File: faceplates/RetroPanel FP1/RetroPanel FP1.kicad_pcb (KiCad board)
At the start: 2 copper layers, 101.5 x 25 mm, 10 parts, among them M1 Mounting_Pin, M10 Mounting_Pad, M2 Mounting_Pin, M3 Mounting_Pin, M4 Mounting_Pin, M5 Mounting_Pad, M6 Mounting_Pad, M7 Mounting_Pad, M8 Mounting_Pad, M9 Mounting_Pad

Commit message: FP1 icons
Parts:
- added G***: LOGO, RetroPanel:logo_small, F.Cu at (150.8, 102.3)
- added G***: LOGO, RetroPanel:icon_extra, F.Cu at (173.5, 97.0)
- added G***: LOGO, RetroPanel:icon_hdd, F.Cu at (177.2, 82.9)
- added G***: LOGO, RetroPanel:icon_running, F.Cu at (120.6, 82.9)
- added G***: LOGO, RetroPanel:icon_slow, F.Cu at (188.2, 82.9)
- added G***: LOGO, RetroPanel:icon_turbo, F.Cu at (184.6, 97.0)
- added G***: LOGO, RetroPanel:icon_power, F.Cu at (116.9, 97.0)
- added G***: LOGO, RetroPanel:icon_reset, F.Cu at (127.9, 97.0)
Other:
- board text removed: "EXTRA"
- board text removed: "POWER"
- board text removed: "RESET"
- board text removed: "TURBO"

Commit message: Export files
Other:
- board text added: "JLCJLCJLCJLC"

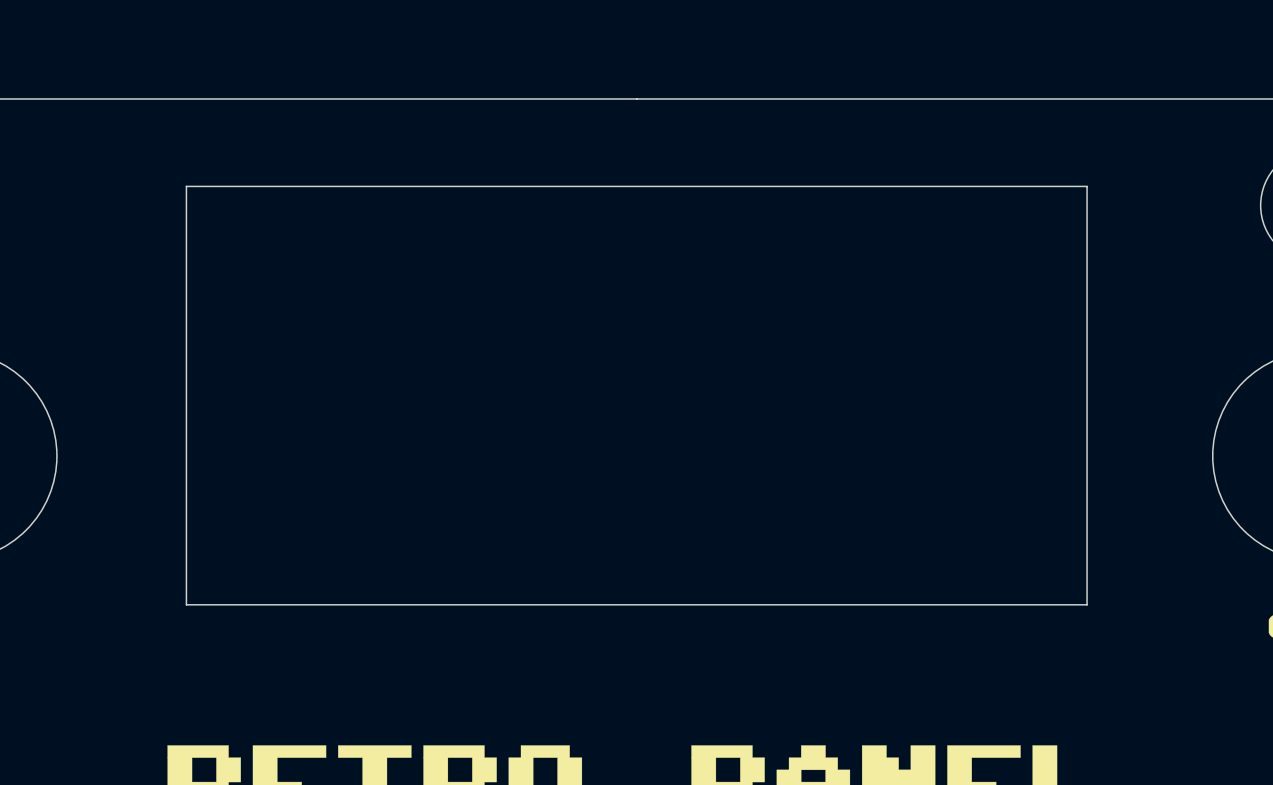
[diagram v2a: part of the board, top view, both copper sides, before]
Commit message: Tweak display cutout
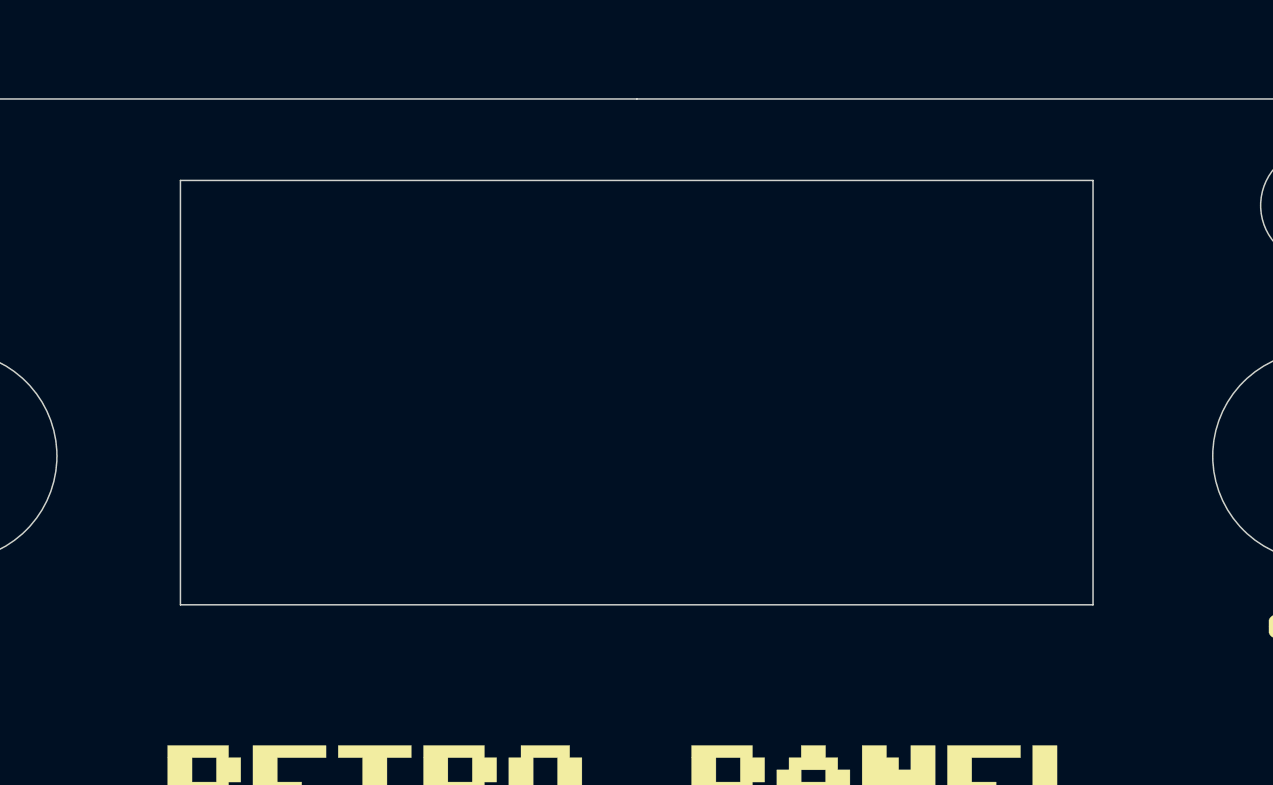
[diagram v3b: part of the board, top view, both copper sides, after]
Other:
- outline, holes or cut-outs redrawn
- board text added: "3.5" RetroPanel Faceplate FP1 (rev. B) github.com/tebl"
- board text removed: "3.5" RetroPanel Faceplate FP1 (rev. A) github.com/tebl"
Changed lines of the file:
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@@
   )
   (gr_circle (center 173.483 82.855) (end 175.383 82.855) (layer Edge.Cuts) (width 0.05))
-  (gr_line (start 135.714 82.22) (end 165.786 82.22) (layer Edge.Cuts) (width 0.05))
-  (gr_line (start 135.714 96.19) (end 135.714 82.22) (layer Edge.Cuts) (width 0.05))
-  (gr_line (start 165.786 96.19) (end 135.714 96.19) (layer Edge.Cuts) (width 0.05))
-  (gr_line (start 165.786 82.22) (end 165.786 96.19) (layer Edge.Cuts) (width 0.05))
+  (gr_line (start 135.514 82.02) (end 165.986 82.02) (layer Edge.Cuts) (width 0.05))
+  (gr_line (start 135.514 96.19) (end 135.514 82.02) (layer Edge.Cuts) (width 0.05))
+  (gr_line (start 165.986 96.19) (end 135.514 96.19) (layer Edge.Cuts) (width 0.05))
+  (gr_line (start 165.986 82.02) (end 165.986 96.19) (layer Edge.Cuts) (width 0.05))
   (gr_circle (center 184.453 82.855) (end 186.353 82.855) (layer Edge.Cuts) (width 0.05))
   (gr_circle (center 116.92 82.855) (end 118.82 82.855) (layer Edge.Cuts) (width 0.05))
@@
   (gr_line (start 112.81 104.3) (end 117.89 104.3) (layer Dwgs.User) (width 0.05))
   (gr_line (start 112.81 101.8) (end 112.81 104.3) (layer Dwgs.User) (width 0.05))
-  (gr_text "3.5\" RetroPanel\nFaceplate FP1 (rev. A)\ngithub.com/tebl" (at 150.75 100.205) (layer B.SilkS)
+  (gr_text "3.5\" RetroPanel\nFaceplate FP1 (rev. B)\ngithub.com/tebl" (at 150.75 100.205) (layer B.SilkS)
     (effects (font (size 0.8 0.8) (thickness 0.1)) (justify mirror))
   )

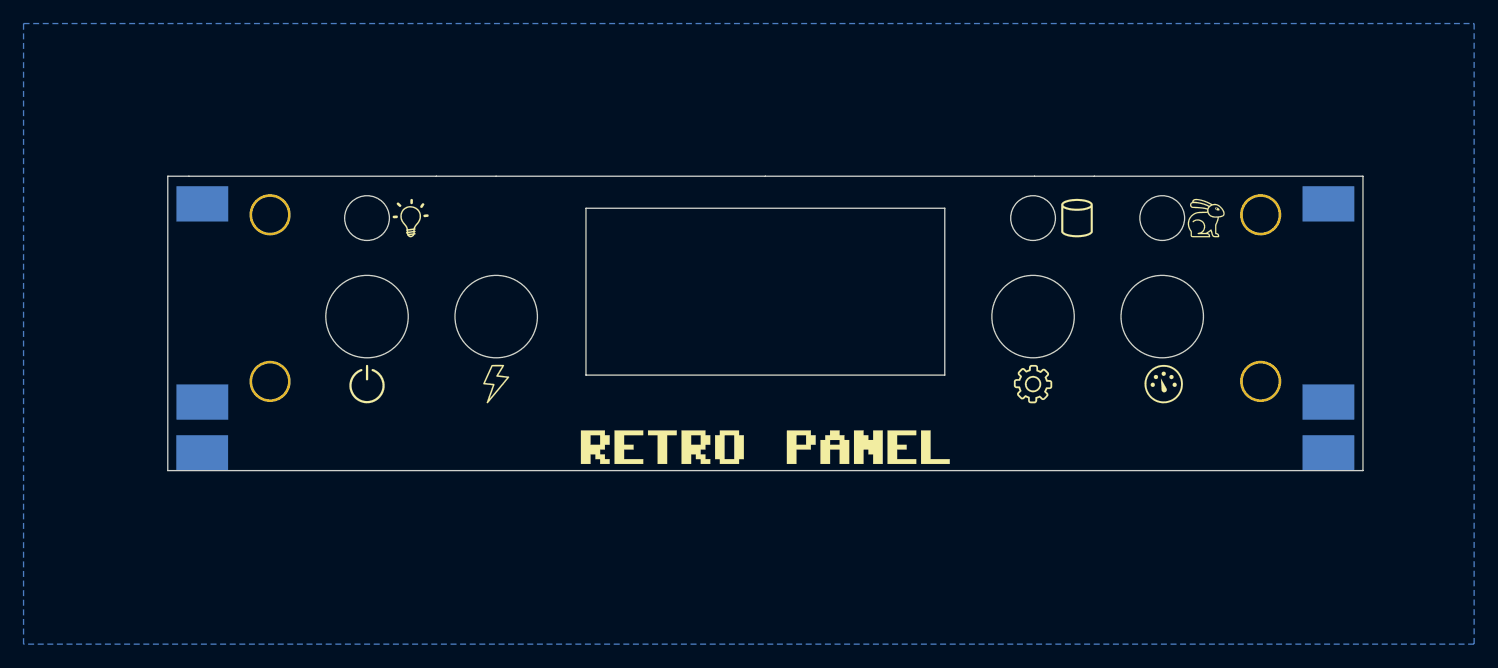
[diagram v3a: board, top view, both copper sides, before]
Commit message: Fixed RS-232 connector and export files for second prototype
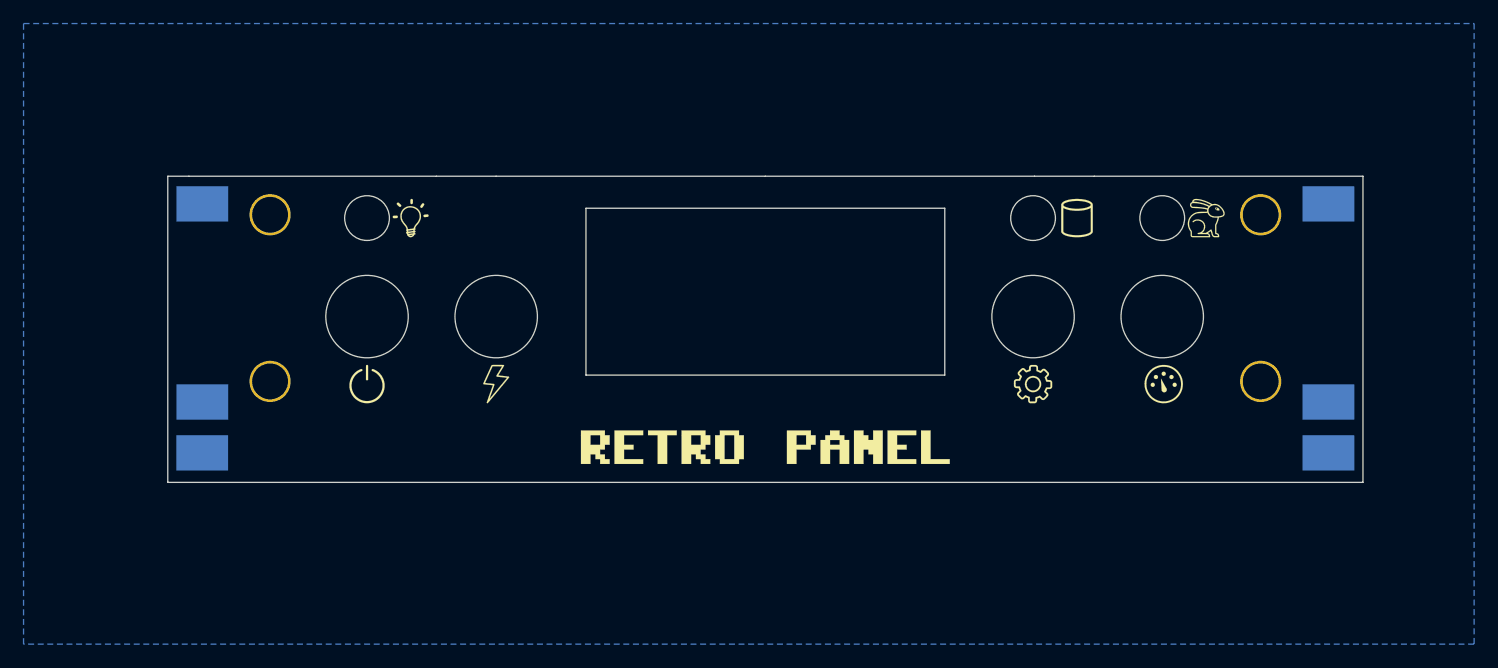
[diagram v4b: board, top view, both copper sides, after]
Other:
- board size 101.5 x 25 mm -> 101.5 x 26 mm

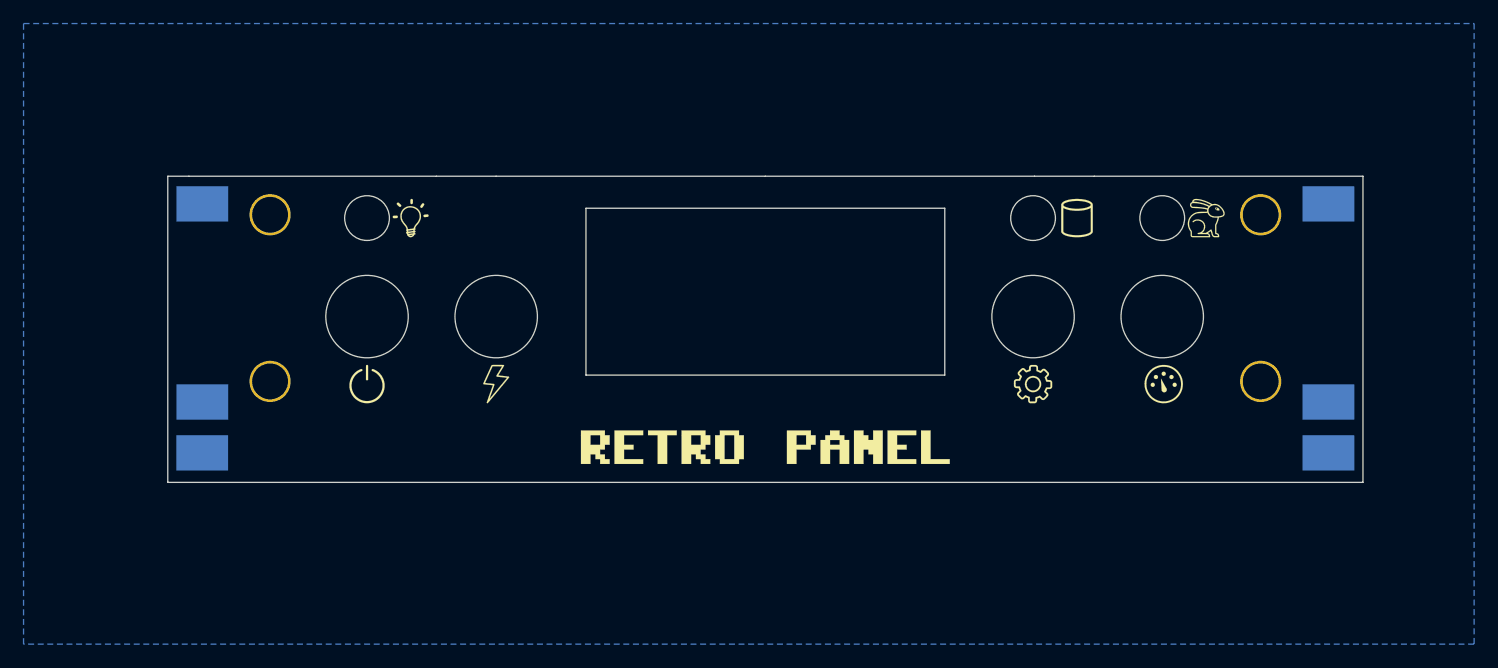
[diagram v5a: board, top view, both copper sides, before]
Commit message: Shorten lower lip
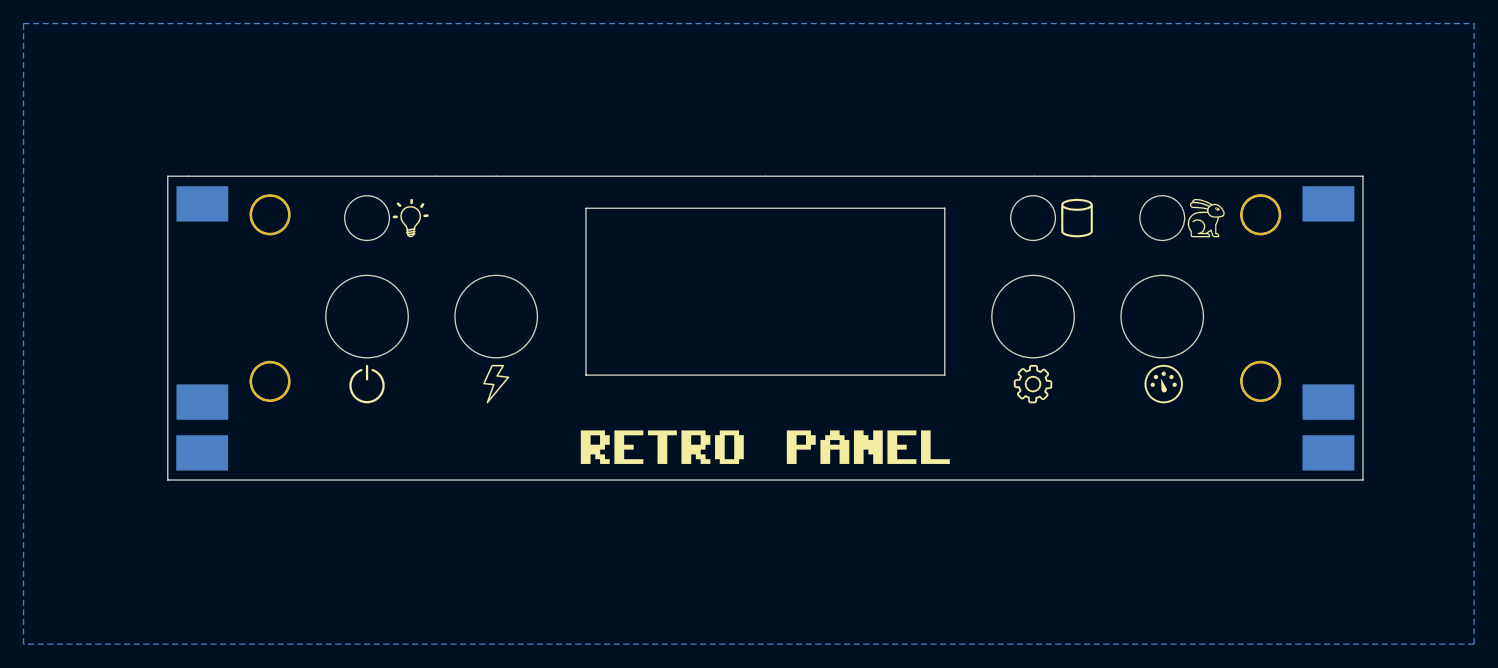
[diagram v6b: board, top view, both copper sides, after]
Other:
- board size 101.5 x 26 mm -> 101.5 x 25.8 mm
- board text added: "3.5" RetroPanel Faceplate FP1 (rev. C) github.com/tebl"
- board text removed: "3.5" RetroPanel Faceplate FP1 (rev. B) github.com/tebl"
